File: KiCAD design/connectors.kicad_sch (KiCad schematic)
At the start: 8 parts, among them J201 Conn_02x19_Odd_Even, J202 Conn_01x03_Female, J203 Conn_01x03_Female, J204 Conn_02x19_Odd_Even, J205 JST BATTERY, J206 JST SENS TOF 2, J208 JST SENS TOF 1, J401 Conn_02x06_Top_Bottom

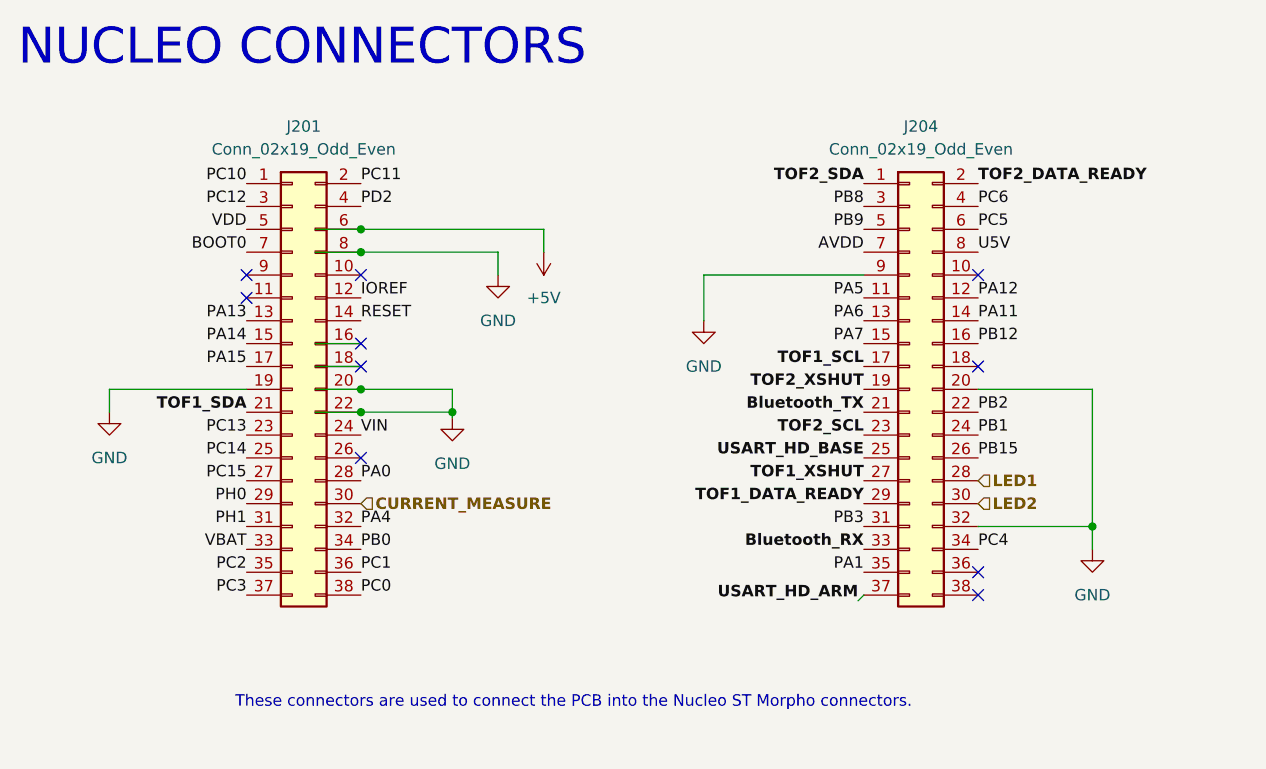
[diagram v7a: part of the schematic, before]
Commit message: change in nucleo pin
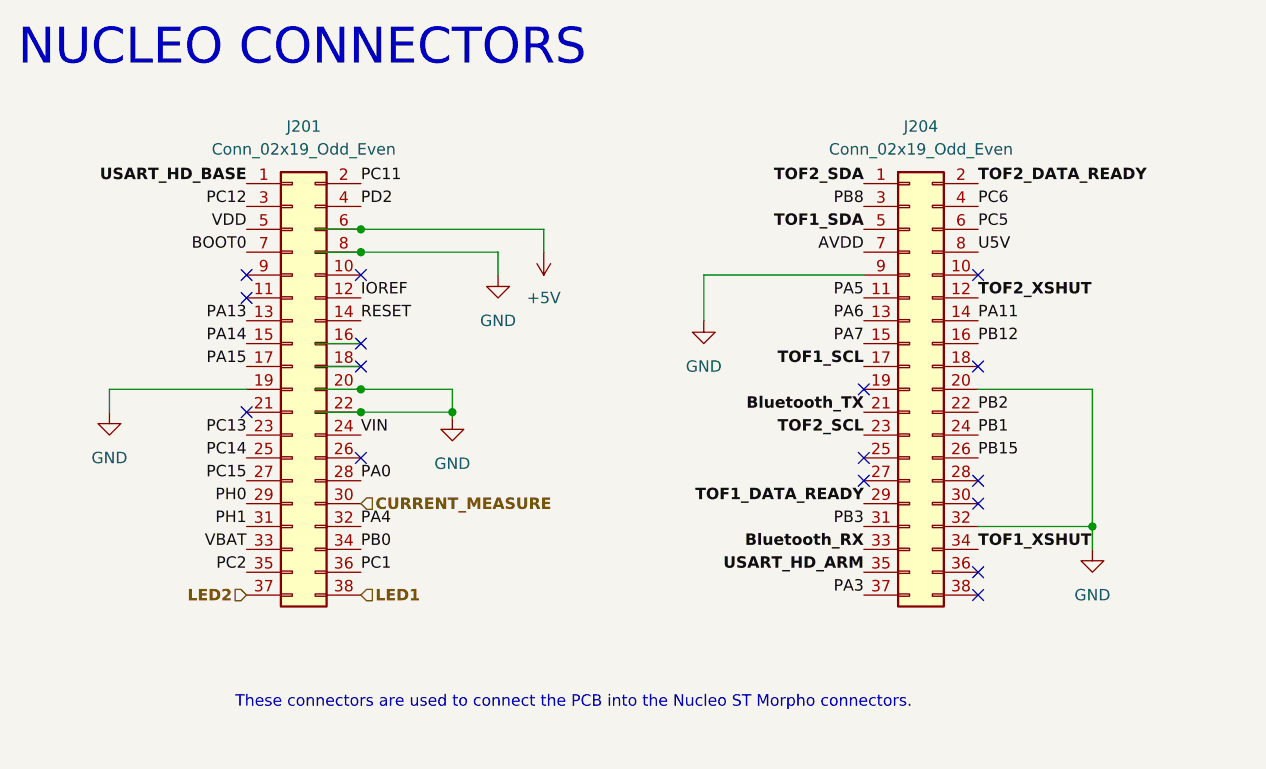
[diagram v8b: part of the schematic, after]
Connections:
- net PA1 is gone; now on net USART_HD_ARM: J204.35 (Pin_35)
- net PA12 is gone; now on net TOF2_XSHUT: J204.12 (Pin_12)
- net PB9 is gone; now on net TOF1_SDA: J204.5 (Pin_5)
- net PC0 is gone; now on net LED1: J201.38 (Pin_38)
- net PC10 is gone; now on net USART_HD_BASE: J201.1 (Pin_1)
- net PC3 is gone; now on net LED2: J201.37 (Pin_37)
- net PC4 is gone; now on net TOF1_XSHUT: J204.34 (Pin_34)
- net LED1: no longer J204.28 (Pin_28)
- net LED2: no longer J204.30 (Pin_30)
- net TOF1_SDA: no longer J201.21 (Pin_21)
- net TOF1_XSHUT: no longer J204.27 (Pin_27)
- net TOF2_XSHUT: no longer J204.19 (Pin_19)
- net USART_HD_ARM: no longer J204.37 (Pin_37)
- net USART_HD_BASE: no longer J204.25 (Pin_25)
- new net PA3: J204.37 (Pin_37)
- no-connect marks 10 -> 16
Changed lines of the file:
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@@
   (no_connect (at 38.1 43.18))
   (no_connect (at 38.1 45.72))
+  (no_connect (at 106.68 63.5))
   (no_connect (at 50.8 50.8))
   (no_connect (at 50.8 43.18))
@@
   (no_connect (at 50.8 63.5))
   (no_connect (at 119.38 43.18))
+  (no_connect (at 106.68 66.04))
+  (no_connect (at 106.68 55.88))
+  (no_connect (at 38.1 58.42))
   (no_connect (at 50.8 53.34))
   (no_connect (at 119.38 53.34))
+  (no_connect (at 119.38 68.58))
+  (no_connect (at 119.38 66.04))
   (wire (pts (xy 43.18 162.56) (xy 43.18 157.48))
     (stroke (width 0) (type default) (color 0 0 0 0))
@@
   )
   (wire (pts (xy 60.96 134.62) (xy 38.1 134.62))
-    (stroke (width 0) (type default) (color 0 0 0 0))
-  )
-  (wire (pts (xy 106.045 79.375) (xy 106.68 78.74))
     (stroke (width 0) (type default) (color 0 0 0 0))
   )
@@
     (effects (font (size 1.27 1.27)) (justify left bottom))
   )
-  (label "PA1" (at 106.68 76.2 180)
-    (effects (font (size 1.27 1.27)) (justify right bottom))
-  )
   (label "VIN" (at 50.8 60.96 0)
     (effects (font (size 1.27 1.27)) (justify left bottom))
@@
     (effects (font (size 1.27 1.27)) (justify left bottom))
   )
-  (label "PB9" (at 106.68 38.1 180)
-    (effects (font (size 1.27 1.27)) (justify right bottom))
-  )
   (label "TOF1_SCL" (at 106.68 53.34 180)
     (effects (font (size 1.27 1.27) (thickness 0.254) bold) (justify right bottom))
   )
-  (label "USART_HD_ARM" (at 106.045 79.375 180)
-    (effects (font (size 1.27 1.27) (thickness 0.254) bold) (justify right bottom))
-  )
-  (label "TOF2_XSHUT" (at 106.68 55.88 180)
-    (effects (font (size 1.27 1.27) (thickness 0.254) bold) (justify right bottom))
-  )
   (label "PB12" (at 119.38 50.8 0)
     (effects (font (size 1.27 1.27)) (justify left bottom))
@@
     (effects (font (size 1.27 1.27)) (justify right bottom))
   )
-  (label "PC4" (at 119.38 73.66 0)
-    (effects (font (size 1.27 1.27)) (justify left bottom))
+  (label "TOF1_XSHUT" (at 119.38 73.66 0)
+    (effects (font (size 1.27 1.27) (thickness 0.254) bold) (justify left bottom))
   )
   (label "PB3" (at 106.68 71.12 180)
@@
   (label "PA6" (at 106.68 48.26 180)
     (effects (font (size 1.27 1.27)) (justify right bottom))
-  )
-  (label "USART_HD_BASE" (at 106.68 63.5 180)
-    (effects (font (size 1.27 1.27) (thickness 0.254) bold) (justify right bottom))
   )
   (label "VBAT" (at 38.1 73.66 180)
@@
     (effects (font (size 1.27 1.27)) (justify right bottom))
   )
-  (label "PA12" (at 119.38 45.72 0)
-    (effects (font (size 1.27 1.27)) (justify left bottom))
-  )
   (label "TOF1_DATA_READY" (at 106.68 68.58 180)
     (effects (font (size 1.27 1.27) (thickness 0.254) bold) (justify right bottom))
@@
     (effects (font (size 1.27 1.27) (thickness 0.254) bold) (justify right bottom))
   )
+  (label "USART_HD_BASE" (at 38.1 33.02 180)
+    (effects (font (size 1.27 1.27) (thickness 0.254) bold) (justify right bottom))
+  )
   (label "PA11" (at 119.38 48.26 0)
     (effects (font (size 1.27 1.27)) (justify left bottom))
@@
     (effects (font (size 1.27 1.27)) (justify right bottom))
   )
-  (label "PC10" (at 38.1 33.02 180)
-    (effects (font (size 1.27 1.27)) (justify right bottom))
-  )
   (label "PC1" (at 50.8 76.2 0)
     (effects (font (size 1.27 1.27)) (justify left bottom))
@@
     (effects (font (size 1.27 1.27)) (justify left bottom))
   )
-  (label "TOF1_SDA" (at 38.1 58.42 180)
-    (effects (font (size 1.27 1.27) (thickness 0.254) bold) (justify right bottom))
-  )
   (label "PA13" (at 38.1 48.26 180)
     (effects (font (size 1.27 1.27)) (justify right bottom))
@@
     (effects (font (size 1.27 1.27)) (justify right bottom))
   )
-  (label "TOF1_XSHUT" (at 106.68 66.04 180)
-    (effects (font (size 1.27 1.27) (thickness 0.254) bold) (justify right bottom))
+  (label "TOF2_XSHUT" (at 119.38 45.72 0)
+    (effects (font (size 1.27 1.27) (thickness 0.254) bold) (justify left bottom))
   )
   (label "TOF2_SCL" (at 106.68 60.96 180)
     (effects (font (size 1.27 1.27) (thickness 0.254) bold) (justify right bottom))
   )
-  (label "PC3" (at 38.1 78.74 180)
-    (effects (font (size 1.27 1.27)) (justify right bottom))
+  (label "TOF1_SDA" (at 106.68 38.1 180)
+    (effects (font (size 1.27 1.27) (thickness 0.254) bold) (justify right bottom))
   )
   (label "Bluetooth_TX" (at 217.17 135.89 180)
@@
     (effects (font (size 1.27 1.27)) (justify right bottom))
   )
+  (label "USART_HD_ARM" (at 106.68 76.2 180)
+    (effects (font (size 1.27 1.27) (thickness 0.254) bold) (justify right bottom))
+  )
   (label "TOF2_XSHUT" (at 198.12 63.5 180)
     (effects (font (size 1.27 1.27)) (justify right bottom))
@@
     (effects (font (size 1.27 1.27)) (justify left bottom))
   )
-  (label "PC0" (at 50.8 78.74 0)
-    (effects (font (size 1.27 1.27)) (justify left bottom))
+  (label "PA3" (at 106.68 78.74 180)
+    (effects (font (size 1.27 1.27)) (justify right bottom))
   )
   (label "PC14" (at 38.1 63.5 180)
@@
   (label "TOF2_SDA" (at 106.68 33.02 180)
     (effects (font (size 1.27 1.27) (thickness 0.254) bold) (justify right bottom))
+  )
+  (hierarchical_label "LED1" (shape input) (at 50.8 78.74 0)
+    (effects (font (size 1.27 1.27) (thickness 0.254) bold) (justify left))
   )
   (hierarchical_label "BATT" (shape input) (at 120.65 145.415 90)
     (effects (font (size 1.27 1.27) bold) (justify left))
   )
-  (hierarchical_label "LED2" (shape input) (at 119.38 68.58 0)
-    (effects (font (size 1.27 1.27) (thickness 0.254) bold) (justify left))
-  )
   (hierarchical_label "CURRENT_MEASURE" (shape input) (at 50.8 68.58 0)
     (effects (font (size 1.27 1.27) (thickness 0.254) bold) (justify left))
   )
-  (hierarchical_label "LED1" (shape input) (at 119.38 66.04 0)
-    (effects (font (size 1.27 1.27) (thickness 0.254) bold) (justify left))
+  (hierarchical_label "LED2" (shape input) (at 38.1 78.74 180)
+    (effects (font (size 1.27 1.27) (thickness 0.254) bold) (justify right))
   )
   (symbol (lib_id "power:+5V") (at 71.12 40.64 180) (unit 1)
